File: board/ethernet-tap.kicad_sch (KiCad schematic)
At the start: 0 parts

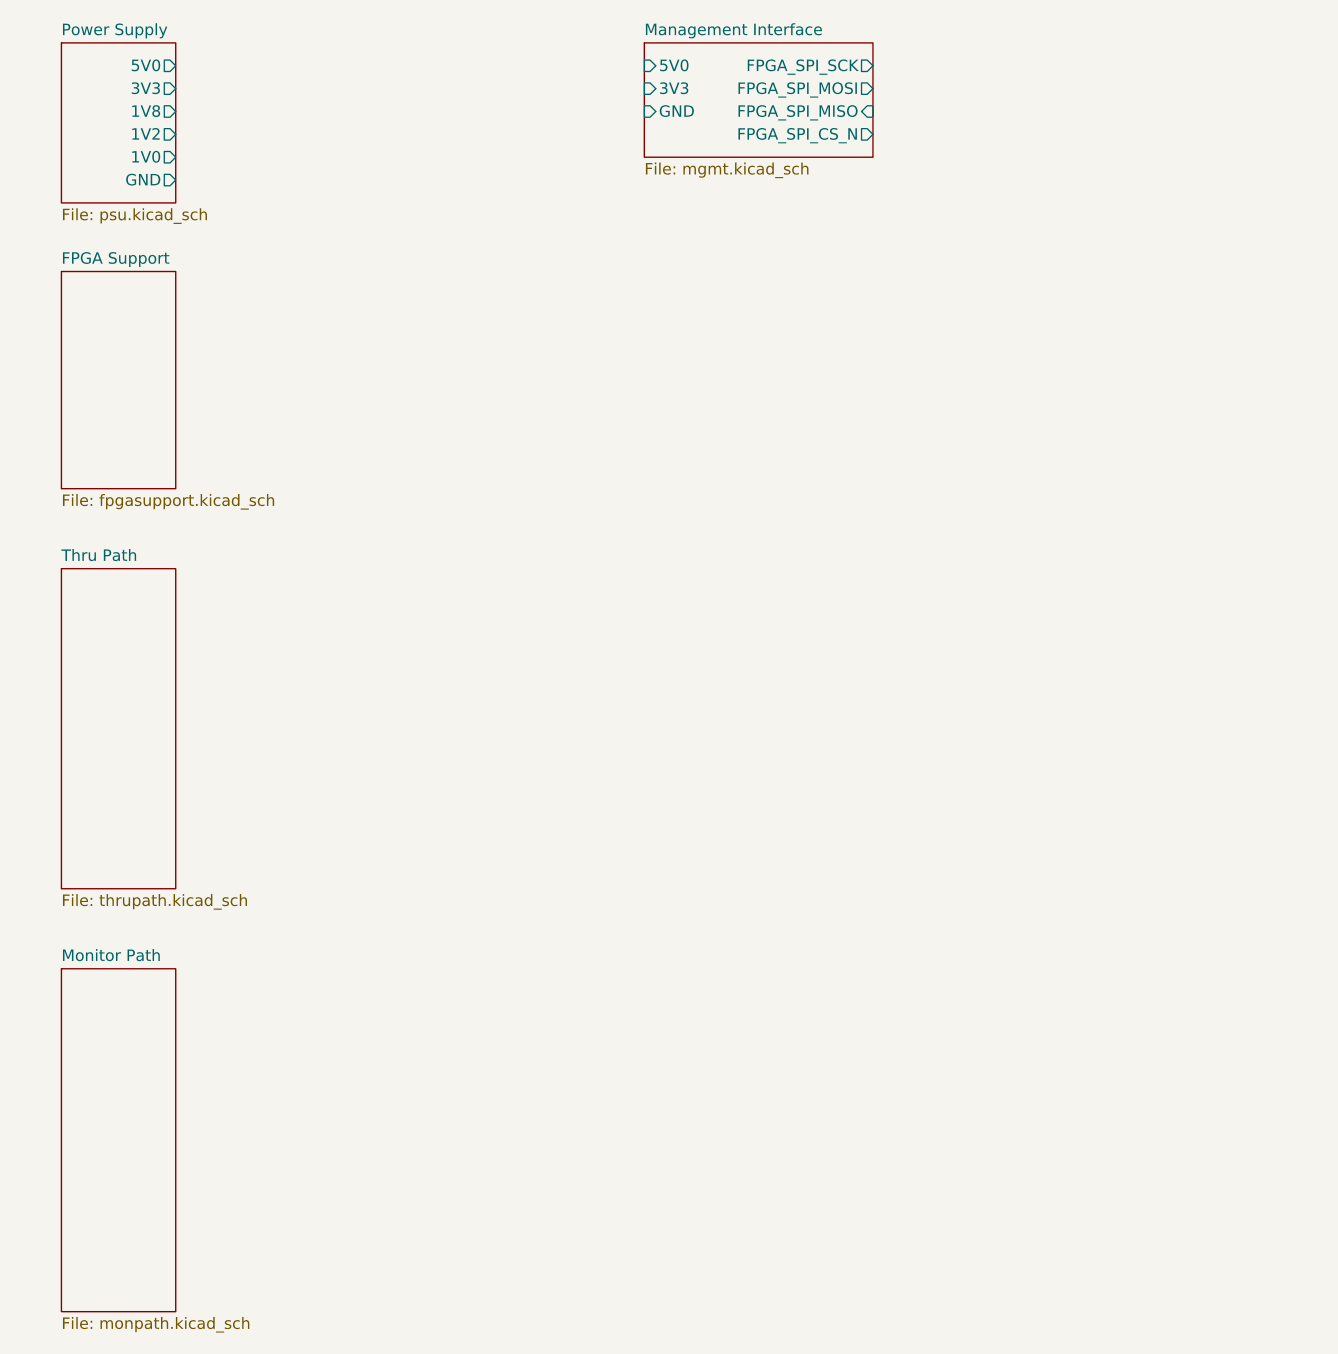
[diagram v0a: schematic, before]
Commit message: Continued initial schematic capture
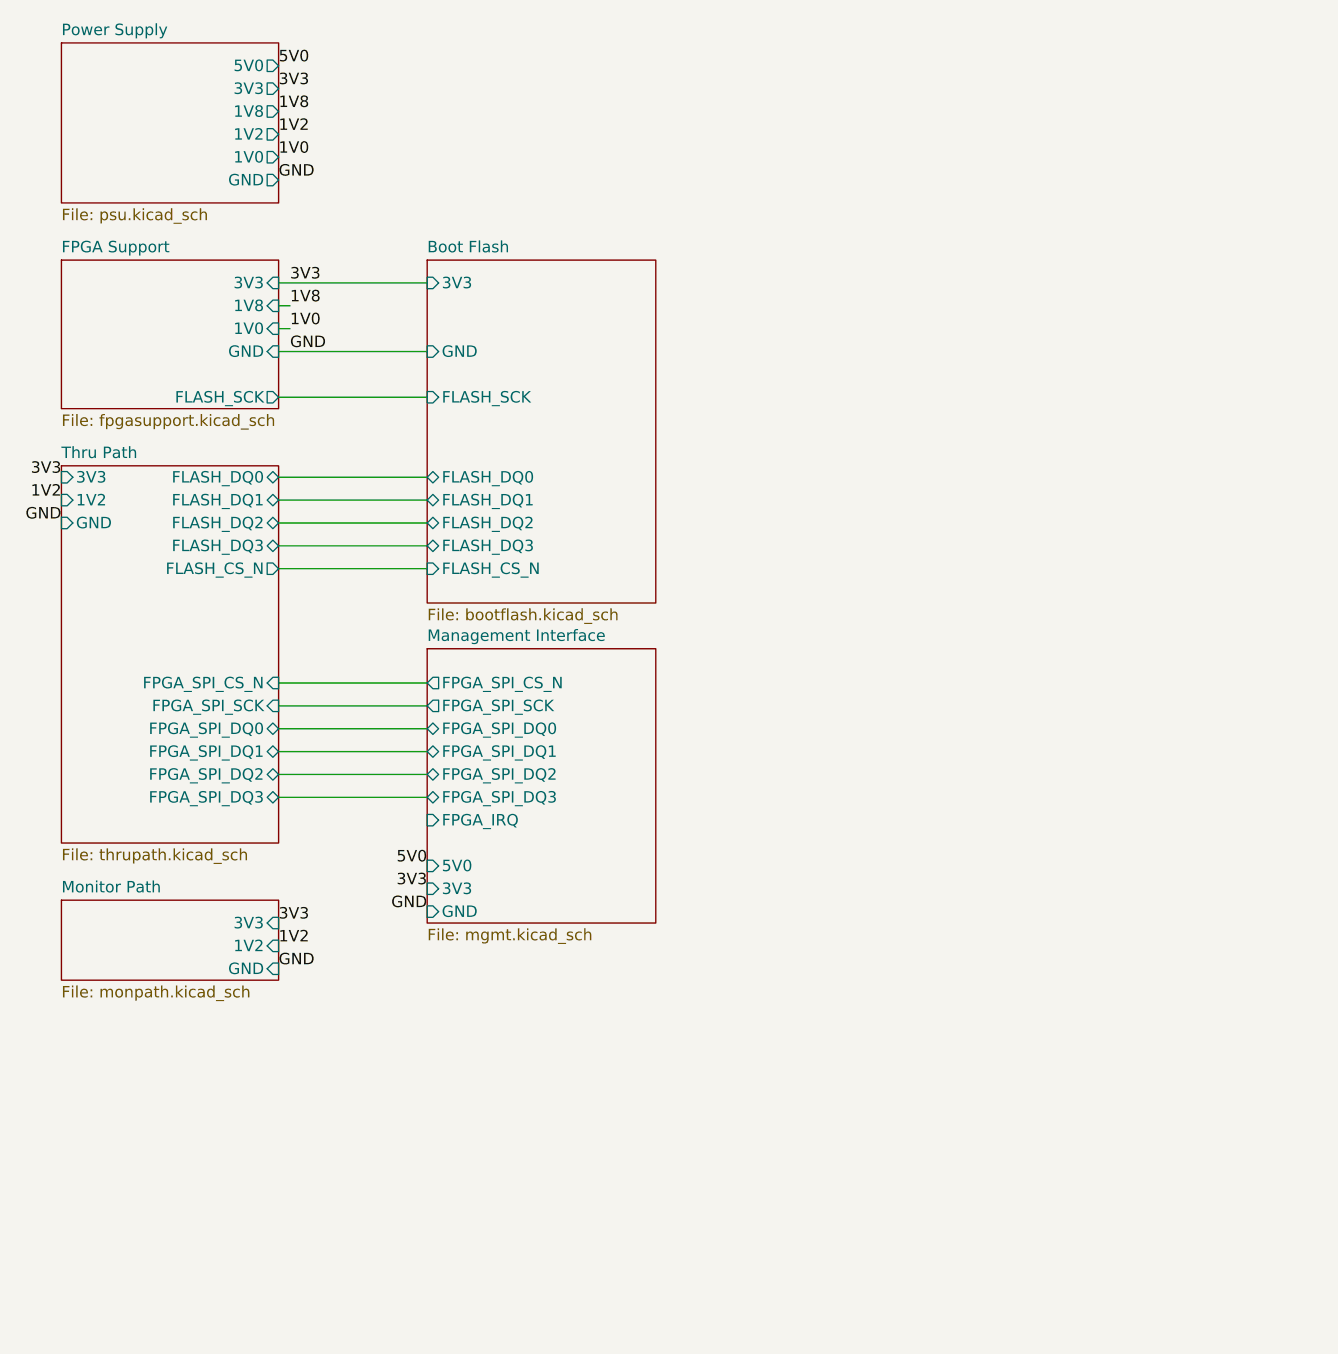
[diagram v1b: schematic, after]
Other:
- added sheet Boot Flash (bootflash.kicad_sch)
- sheet FPGA Support ports: added 1V0, 1V8, 3V3, FLASH_SCK, GND; removed none
- sheet Management Interface ports: added FPGA_IRQ, FPGA_SPI_DQ0, FPGA_SPI_DQ1, FPGA_SPI_DQ2, FPGA_SPI_DQ3; removed FPGA_SPI_MISO, FPGA_SPI_MOSI
- sheet Monitor Path ports: added 1V2, 3V3, GND; removed none
- sheet Thru Path ports: added 1V2, 3V3, FLASH_CS_N, FLASH_DQ0, FLASH_DQ1, FLASH_DQ2, FLASH_DQ3, FPGA_SPI_CS_N, FPGA_SPI_DQ0, FPGA_SPI_DQ1, FPGA_SPI_DQ2, FPGA_SPI_DQ3, FPGA_SPI_SCK, GND; removed none

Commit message: Finished initial schematic, ready for signoff review
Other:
- sheet Thru Path ports: added FPGA_IRQ; removed none

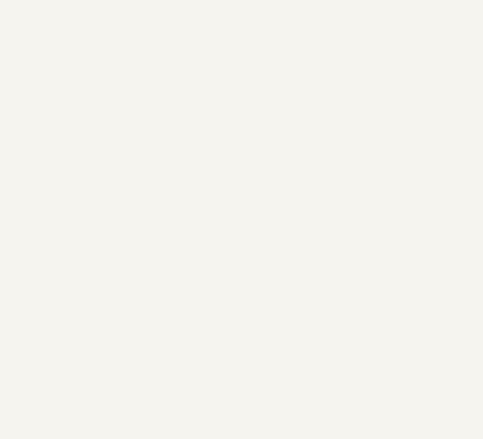
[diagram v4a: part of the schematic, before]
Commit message: Finished power supply layout, added mounting holes and a bunch of silkscreen labeling
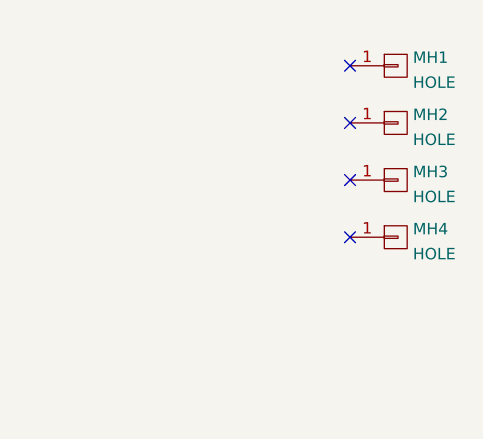
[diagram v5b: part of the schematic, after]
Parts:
- added MH1, MH2, MH3, MH4: HOLE, azonenberg_pcb:MECHANICAL_CLEARANCEHOLE_4_40, symbol conn:CONN_01X01
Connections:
- no-connect marks 0 -> 4
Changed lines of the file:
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@@
   (title_block
     (title "Active 10/100/1000baseT Tap")
-    (date "2022-12-21")
+    (date "2022-12-23")
     (rev "0.1")
     (company "Antikernel Labs")
     (comment 1 "Andrew D. Zonenberg")
   )
+  (no_connect (at 157.48 39.37))
+  (no_connect (at 157.48 33.02))
+  (no_connect (at 157.48 45.72))
+  (no_connect (at 157.48 26.67))
   (wire (pts (xy 54.61 80.01) (xy 71.12 80.01))
     (stroke (width 0) (type default) (color 0 0 0 0))
@@
   (label "3V3" (at 55.88 50.8 0)
     (effects (font (size 1.27 1.27)) (justify left bottom))
+  )
+  (symbol (lib_id "conn:CONN_01X01") (at 162.56 33.02 0) (unit 1)
+    (in_bom yes) (on_board yes) (fields_autoplaced)
+    (property "Reference" "MH2" (id 0) (at 164.465 32.1115 0)
+      (effects (font (size 1.27 1.27)) (justify left))
+    )
+    (property "Value" "HOLE" (id 1) (at 164.465 34.8866 0)
+      (effects (font (size 1.27 1.27)) (justify left))
+    )
+    (property "Footprint" "azonenberg_pcb:MECHANICAL_CLEARANCEHOLE_4_40" (id 2) (at 162.56 33.02 0)
+      (effects (font (size 1.27 1.27)) hide)
+    )
+    (property "Datasheet" "" (id 3) (at 162.56 33.02 0)
+      (effects (font (size 1.27 1.27)) hide)
+    )
+    (pin "1")
+  )
+  (symbol (lib_id "conn:CONN_01X01") (at 162.56 26.67 0) (unit 1)
+    (in_bom yes) (on_board yes) (fields_autoplaced)
+    (property "Reference" "MH1" (id 0) (at 164.465 25.7615 0)
+      (effects (font (size 1.27 1.27)) (justify left))
+    )
+    (property "Value" "HOLE" (id 1) (at 164.465 28.5366 0)
+      (effects (font (size 1.27 1.27)) (justify left))
+    )
+    (property "Footprint" "azonenberg_pcb:MECHANICAL_CLEARANCEHOLE_4_40" (id 2) (at 162.56 26.67 0)
+      (effects (font (size 1.27 1.27)) hide)
+    )
+    (property "Datasheet" "" (id 3) (at 162.56 26.67 0)
+      (effects (font (size 1.27 1.27)) hide)
+    )
+    (pin "1")
+  )
+  (symbol (lib_id "conn:CONN_01X01") (at 162.56 45.72 0) (unit 1)
+    (in_bom yes) (on_board yes) (fields_autoplaced)
+    (property "Reference" "MH4" (id 0) (at 164.465 44.8115 0)
+      (effects (font (size 1.27 1.27)) (justify left))
+    )
+    (property "Value" "HOLE" (id 1) (at 164.465 47.5866 0)
+      (effects (font (size 1.27 1.27)) (justify left))
+    )
+    (property "Footprint" "azonenberg_pcb:MECHANICAL_CLEARANCEHOLE_4_40" (id 2) (at 162.56 45.72 0)
+      (effects (font (size 1.27 1.27)) hide)
+    )
+    (property "Datasheet" "" (id 3) (at 162.56 45.72 0)
+      (effects (font (size 1.27 1.27)) hide)
+    )
+    (pin "1")
+  )
+  (symbol (lib_id "conn:CONN_01X01") (at 162.56 39.37 0) (unit 1)
+    (in_bom yes) (on_board yes) (fields_autoplaced)
+    (property "Reference" "MH3" (id 0) (at 164.465 38.4615 0)
+      (effects (font (size 1.27 1.27)) (justify left))
+    )
+    (property "Value" "HOLE" (id 1) (at 164.465 41.2366 0)
+      (effects (font (size 1.27 1.27)) (justify left))
+    )
+    (property "Footprint" "azonenberg_pcb:MECHANICAL_CLEARANCEHOLE_4_40" (id 2) (at 162.56 39.37 0)
+      (effects (font (size 1.27 1.27)) hide)
+    )
+    (property "Datasheet" "" (id 3) (at 162.56 39.37 0)
+      (effects (font (size 1.27 1.27)) hide)
+    )
+    (pin "1")
   )
   (sheet (at 71.12 91.44) (size 25.4 30.48) (fields_autoplaced)
@@
       (reference "L5") (unit 1) (value "2.2 uH") (footprint "azonenberg_pcb:EIA_1210_CAP_NOSILK")
     )
+    (path "/5b1f3045-a75d-4b94-9b4b-27839038f840"
+      (reference "MH1") (unit 1) (value "HOLE") (footprint "azonenberg_pcb:MECHANICAL_CLEARANCEHOLE_4_40")
+    )
+    (path "/356ddd81-1842-48a4-bdc0-c842f28b6ff9"
+      (reference "MH2") (unit 1) (value "HOLE") (footprint "azonenberg_pcb:MECHANICAL_CLEARANCEHOLE_4_40")
+    )
+    (path "/814c72ad-2124-442c-a182-323903fee0f7"
+      (reference "MH3") (unit 1) (value "HOLE") (footprint "azonenberg_pcb:MECHANICAL_CLEARANCEHOLE_4_40")
+    )
+    (path "/6b289472-2d4d-434e-a2f6-ff5bac177332"
+      (reference "MH4") (unit 1) (value "HOLE") (footprint "azonenberg_pcb:MECHANICAL_CLEARANCEHOLE_4_40")
+    )
     (path "/cada0bea-1c13-43de-8c76-f71887adf217/28f8a272-ad05-49f0-b9f0-48cb70ea1d36"
